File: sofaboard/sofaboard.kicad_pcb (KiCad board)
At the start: 2 copper layers, 179 parts, among them J1 USB_B_Micro, SW1 SW_Push, SW10 SW_Push, SW11 SW_Push, SW12 SW_Push, SW13 SW_Push, SW14 SW_Push, SW15 SW_Push, SW16 SW_Push, SW17 SW_Push, SW18 SW_Push, SW19 SW_Push, SW2 SW_Push, SW20 SW_Push, SW21 SW_Push, SW22 SW_Push, SW23 SW_Push, SW24 SW_Push, SW25 SW_Push, SW26 SW_Push, SW27 SW_Push, SW28 SW_Push, SW29 SW_Push, SW3 SW_Push, SW30 SW_Push, SW31 SW_Push, SW32 SW_Push, SW33 SW_Push, SW34 SW_Push, SW35 SW_Push, SW36 SW_Push, SW37 SW_Push, SW38 SW_Push, SW39 SW_Push, SW4 SW_Push, SW40 SW_Push, SW41 SW_Push, SW42 SW_Push, SW43 SW_Push, SW44 SW_Push, SW45 SW_Push, SW46 SW_Push, SW47 SW_Push, SW48 SW_Push, SW49 SW_Push, SW5 SW_Push, SW50 SW_Push, SW51 SW_Push, SW52 SW_Push, SW53 SW_Push, SW54 SW_Push, SW55 SW_Push, SW56 SW_Push, SW57 SW_Push, SW58 SW_Push, SW59 SW_Push, SW6 SW_Push, SW60 SW_Push, SW61 SW_Push, SW62 SW_Push, SW63 SW_Push, SW64 SW_Push, SW65 SW_Push, SW66 SW_Push, SW67 SW_Push, SW68 SW_Push, SW69 SW_Push, SW7 SW_Push, SW70 SW_Push, SW71 SW_Push, SW72 SW_Push, SW73 SW_Push, SW74 SW_Push, SW75 SW_Push, SW76 SW_Push, SW77 SW_Push, SW78 SW_Push, SW79 SW_Push, SW8 SW_Push, SW80 SW_Push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

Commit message: Comonent Placement
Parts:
- C1, C2, C3, C4, C5, C6, C7, C8, D1, D10, D11, D12, D13, D14, D15, D16, D17, D18, D19, D2, D20, D21, D22, D23, D24, D25, D26, D27, D28, D29, D3, D30, D31, D32, D33, D34, D35, D36, D37, D38, D39, D4, D40, D41, D42, D43, D44, D45, D46, D47, D48, D49, D5, D50, D51, D52, D53, D54, D55, D56, D57, D58, D59, D6, D60, D61, D62, D63, D64, D65, D66, D67, D68, D69, D7, D70, D71, D72, D73, D74, D75, D76, D77, D78, D79, D8, D80, D81, D82, D9, J1, R1, R2, R3, SW83, U1, Y1: moved to B.Cu
- moved R3 632.6 mm to (289.2, -111.5), turned to 90 degrees
- moved R1 619.5 mm to (285.9, -111.5), turned to 90 degrees
- moved R2 602.3 mm to (292.7, -46.0), turned to 180 degrees
- moved D14 600.2 mm to (301.4, -109.7), turned to 180 degrees
- moved C2 595.7 mm to (283.9, -68.2), turned to 270 degrees
- moved D72 588.8 mm to (282.3, -33.5), turned to 180 degrees
- moved C7 581.6 mm to (266.2, -47.3), turned to 180 degrees
- moved D43 581.5 mm to (277.3, -72.5), turned to 180 degrees
- moved D73 576.6 mm to (301.4, -33.5), turned to 180 degrees
- moved Y1 571.2 mm to (291.4, -91.9), turned to 270 degrees
- moved D13 559.1 mm to (272.7, -109.6), turned to 180 degrees
- moved D70 554.1 mm to (244.2, -33.4), turned to 180 degrees
- moved D58 553.0 mm to (301.3, -52.5), turned to 180 degrees
- moved D12 544.1 mm to (253.7, -109.7), turned to 180 degrees
- moved D44 542.6 mm to (301.3, -71.5), turned to 180 degrees
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
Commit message: Started layouting
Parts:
- moved Y1 31.9 mm to (262.7, -77.9)
- moved C7 30.7 mm to (296.9, -46.7), turned to 270 degrees
- moved R2 26.7 mm to (287.7, -72.2), turned to 90 degrees
- moved C6 24.5 mm to (294.6, -48.4)
- moved C2 22.4 mm to (267.9, -83.9), turned to 180 degrees
- moved C1 19.1 mm to (292.5, -48.4)
- moved C4 19.0 mm to (296.9, -55.4), turned to 0 degrees
- moved C5 14.7 mm to (287.1, -48.4)
- moved C3 13.6 mm to (275.2, -56.2), turned to 90 degrees
- moved C8 13.5 mm to (290.3, -48.4)
- moved SW83 11.8 mm to (291.0, -81.9)
- moved U1 2.45 mm to (285.9, -59.6), turned to 90 degrees
- moved R3 1.15 mm to (288.1, -111.5)
- moved R1 0.20 mm to (286.1, -111.5)
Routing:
- net row1: track 0.00 -> 553.8 mm, vias 0 -> 2
- net row3: track 0.00 -> 468.8 mm, vias 0 -> 2
- net row5: track 0.00 -> 453.1 mm, vias 0 -> 2
- net row0: track 0.00 -> 411.5 mm, vias 0 -> 2
- net row2: track 0.00 -> 399.2 mm, vias 0 -> 2
- net col0: track 0.00 -> 368.0 mm, vias 0 -> 2
- net col1: track 0.00 -> 353.9 mm, vias 0 -> 5
- net row4: track 0.00 -> 342.1 mm
- net col2: track 0.00 -> 337.2 mm, vias 0 -> 3
- net col6: track 0.00 -> 319.7 mm, vias 0 -> 4
- net col5: track 0.00 -> 303.6 mm, vias 0 -> 3
- net col3: track 0.00 -> 301.8 mm, vias 0 -> 5
- net col4: track 0.00 -> 268.4 mm, vias 0 -> 1
- net col7: track 0.00 -> 256.2 mm, vias 0 -> 4
- net col10: track 0.00 -> 236.4 mm, vias 0 -> 1
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
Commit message: Optimised routing
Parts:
- moved SW83 174.2 mm to (129.4, -16.8)
- moved C4 137.0 mm to (165.9, -15.2), turned to 180 degrees
- moved C2 127.6 mm to (152.5, -29.6), turned to 270 degrees
- moved C5 124.0 mm to (166.0, -21.8), turned to 180 degrees
- moved C3 119.9 mm to (161.3, -18.6), turned to 270 degrees
- moved Y1 119.6 mm to (156.7, -22.7)
- moved U1 113.3 mm to (178.6, -23.0), turned to 0 degrees
- moved R2 110.2 mm to (190.2, -21.1), turned to 0 degrees
- moved C7 105.7 mm to (194.4, -21.1), turned to 0 degrees
- moved C6 104.5 mm to (194.4, -18.9), turned to 0 degrees
- moved C1 103.1 mm to (194.4, -16.8), turned to 0 degrees
- moved C8 101.7 mm to (194.4, -14.6), turned to 0 degrees
- moved J1 86.1 mm to (201.0, -118.4)
- moved R1 86.1 mm to (200.0, -110.7)
- moved R3 86.1 mm to (202.0, -110.7)
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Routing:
- net col5: track 303.6 -> 139.8 mm, vias 3 -> 1
- net col6: track 319.7 -> 163.6 mm, vias 4 -> 1
- net col7: track 256.2 -> 114.6 mm, vias 4 -> 1
- net col8: track 204.5 -> 95.2 mm, vias 4 -> 0
- net col3: track 301.8 -> 196.9 mm, vias 5 -> 1
- net col14: track 122.3 -> 225.4 mm, vias 2 -> 0
- net col2: track 337.2 -> 235.0 mm, vias 3 -> 1
- net col1: track 353.9 -> 252.8 mm, vias 5 -> 0
- net col10: track 236.4 -> 138.9 mm
- net col0: track 368.0 -> 272.8 mm, vias 2 -> 1
- net col4: track 268.4 -> 179.7 mm
- net col9: track 206.8 -> 119.4 mm, vias 3 -> 1
- net Net-(R3-Pad1): track 65.1 -> 150.5 mm
- net Net-(R1-Pad1): track 63.4 -> 146.6 mm
- net col13: track 122.3 -> 204.1 mm, vias 0 -> 1
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
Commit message: Added GND planes
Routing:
- net +5V: track 53.2 -> 152.8 mm, vias 0 -> 4
- net GND: track 0.00 -> 13.0 mm, vias 0 -> 25
- net (no net): vias 0 -> 1
- added copper zone on B.Cu, net GND
- added copper zone on F.Cu, net GND
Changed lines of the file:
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@@
     (thickness 1.6)
     (drawings 364)
-    (tracks 957)
+    (tracks 1014)
     (zones 0)
     (modules 179)
@@
     (0 F.Cu signal)
     (31 B.Cu signal)
-    (32 B.Adhes user hide)
-    (33 F.Adhes user hide)
-    (34 B.Paste user hide)
-    (35 F.Paste user hide)
-    (36 B.SilkS user hide)
-    (37 F.SilkS user hide)
-    (38 B.Mask user hide)
-    (39 F.Mask user hide)
-    (40 Dwgs.User user hide)
-    (41 Cmts.User user hide)
-    (42 Eco1.User user hide)
-    (43 Eco2.User user hide)
-    (44 Edge.Cuts user hide)
-    (45 Margin user hide)
-    (46 B.CrtYd user hide)
-    (47 F.CrtYd user hide)
-    (48 B.Fab user hide)
-    (49 F.Fab user hide)
+    (32 B.Adhes user)
+    (33 F.Adhes user)
+    (34 B.Paste user)
+    (35 F.Paste user)
+    (36 B.SilkS user)
+    (37 F.SilkS user)
+    (38 B.Mask user)
+    (39 F.Mask user)
+    (40 Dwgs.User user)
+    (41 Cmts.User user)
+    (42 Eco1.User user)
+    (43 Eco2.User user)
+    (44 Edge.Cuts user)
+    (45 Margin user)
+    (46 B.CrtYd user)
+    (47 F.CrtYd user)
+    (48 B.Fab user)
+    (49 F.Fab user)
   )
   (setup
@@
   (gr_line (start 122.841 -121.9501) (end 136.842 -121.9501) (layer Dwgs.User) (width 0.2))
   (gr_line (start 227.33 -50.8) (end 213.33 -50.8) (layer Dwgs.User) (width 0.2))
+  (via (at 179.29 -22.57) (size 0.8) (drill 0.4) (layers F.Cu B.Cu) (net 0))
   (segment (start 193.36 -18.945) (end 193.335 -18.92) (width 0.25) (layer B.Cu) (net 1))
   (segment (start 193.36 -21.05) (end 193.36 -18.945) (width 0.25) (layer B.Cu) (net 1))
@@
   (segment (start 193.34 -16.765) (end 193.355 -16.78) (width 0.25) (layer B.Cu) (net 1))
   (segment (start 193.34 -14.59) (end 193.34 -16.765) (width 0.25) (layer B.Cu) (net 1))
+  (via (at 176.69 -37.5) (size 0.8) (drill 0.4) (layers F.Cu B.Cu) (net 1))
+  (segment (start 175.83 -30.73) (end 175.83 -36.64) (width 0.25) (layer B.Cu) (net 1))
+  (segment (start 175.83 -36.64) (end 176.69 -37.5) (width 0.25) (layer B.Cu) (net 1))
+  (via (at 187.52 -81.27) (size 0.8) (drill 0.4) (layers F.Cu B.Cu) (net 1))
+  (segment (start 187.52 -43.510998) (end 187.52 -81.27) (width 0.25) (layer F.Cu) (net 1))
+  (segment (start 176.69 -37.5) (end 181.509002 -37.5) (width 0.25) (layer F.Cu) (net 1))
+  (segment (start 181.509002 -37.5) (end 187.52 -43.510998) (width 0.25) (layer F.Cu) (net 1))
+  (segment (start 187.52 -81.27) (end 193.89 -87.64) (width 0.25) (layer B.Cu) (net 1))
+  (via (at 192.69 -102.84) (size 0.8) (drill 0.4) (layers F.Cu B.Cu) (net 1))
+  (segment (start 193.89 -87.64) (end 193.89 -101.64) (width 0.25) (layer B.Cu) (net 1))
+  (segment (start 193.89 -101.64) (end 192.69 -102.84) (width 0.25) (layer B.Cu) (net 1))
+  (via (at 198.23 -113.23) (size 0.8) (drill 0.4) (layers F.Cu B.Cu) (net 1))
+  (segment (start 192.69 -102.84) (end 198.23 -108.38) (width 0.25) (layer F.Cu) (net 1))
+  (segment (start 198.23 -108.38) (end 198.23 -113.23) (width 0.25) (layer F.Cu) (net 1))
+  (segment (start 199.67 -114.67) (end 199.67 -116.64) (width 0.25) (layer B.Cu) (net 1))
+  (segment (start 198.23 -113.23) (end 199.67 -114.67) (width 0.25) (layer B.Cu) (net 1))
+  (via (at 150.14 -20.2) (size 0.8) (drill 0.4) (layers F.Cu B.Cu) (net 2))
+  (via (at 160.47 -21.73) (size 0.8) (drill 0.4) (layers F.Cu B.Cu) (net 2))
+  (via (at 172.8 -37.19) (size 0.8) (drill 0.4) (layers F.Cu B.Cu) (net 2))
+  (segment (start 176.63 -31.73) (end 176.6 -31.76) (width 0.25) (layer B.Cu) (net 2))
+  (segment (start 176.63 -30.73) (end 176.63 -31.73) (width 0.25) (layer B.Cu) (net 2))
+  (via (at 179.54 -18.15) (size 0.8) (drill 0.4) (layers F.Cu B.Cu) (net 2))
+  (segment (start 181.43 -15.33) (end 181.43 -16.91) (width 0.25) (layer B.Cu) (net 2))
+  (via (at 180.02 -26.42) (size 0.8) (drill 0.4) (layers F.Cu B.Cu) (net 2))
+  (via (at 174.04 -26.26) (size 0.8) (drill 0.4) (layers F.Cu B.Cu) (net 2))
+  (segment (start 173.43 -16.33) (end 173.42 -16.34) (width 0.25) (layer B.Cu) (net 2))
+  (segment (start 173.43 -15.33) (end 173.43 -16.33) (width 0.25) (layer B.Cu) (net 2))
+  (segment (start 173.43 -16.33) (end 173.43 -16.79) (width 0.25) (layer B.Cu) (net 2))
+  (segment (start 169.93 -21.03) (end 169.68 -20.78) (width 0.25) (layer B.Cu) (net 2))
+  (segment (start 170.93 -21.03) (end 169.93 -21.03) (width 0.25) (layer B.Cu) (net 2))
+  (segment (start 169.68 -20.78) (end 165.02 -20.78) (width 0.25) (layer B.Cu) (net 2))
+  (segment (start 164.965 -20.835) (end 164.965 -21.83) (width 0.25) (layer B.Cu) (net 2))
+  (segment (start 165.02 -20.78) (end 164.965 -20.835) (width 0.25) (layer B.Cu) (net 2))
+  (segment (start 165.02 -20.78) (end 164.94 -20.78) (width 0.25) (layer B.Cu) (net 2))
+  (segment (start 176.63 -29.73) (end 176.64 -29.72) (width 0.25) (layer B.Cu) (net 2))
+  (segment (start 176.63 -30.73) (end 176.63 -29.73) (width 0.25) (layer B.Cu) (net 2))
+  (segment (start 176.64 -29.72) (end 176.64 -28.98) (width 0.25) (layer B.Cu) (net 2))
+  (via (at 188.87 -15.25) (size 0.8) (drill 0.4) (layers F.Cu B.Cu) (net 2))
+  (via (at 190.92 -17.76) (size 0.8) (drill 0.4) (layers F.Cu B.Cu) (net 2))
+  (via (at 158.98 -15.54) (size 0.8) (drill 0.4) (layers F.Cu B.Cu) (net 2))
+  (via (at 158.9 -18.06) (size 0.8) (drill 0.4) (layers F.Cu B.Cu) (net 2))
+  (via (at 190.79 -32.93) (size 0.8) (drill 0.4) (layers F.Cu B.Cu) (net 2))
+  (via (at 228.92 -22.65) (size 0.8) (drill 0.4) (layers F.Cu B.Cu) (net 2))
+  (via (at 251.56 -22.73) (size 0.8) (drill 0.4) (layers F.Cu B.Cu) (net 2))
+  (via (at 272.28 -23.4) (size 0.8) (drill 0.4) (layers F.Cu B.Cu) (net 2))
+  (via (at 290.75 -22.49) (size 0.8) (drill 0.4) (layers F.Cu B.Cu) (net 2))
+  (via (at 32.07 -23.6) (size 0.8) (drill 0.4) (layers F.Cu B.Cu) (net 2))
+  (via (at 51.96 -23.16) (size 0.8) (drill 0.4) (layers F.Cu B.Cu) (net 2))
+  (via (at 151.69 -14.03) (size 0.8) (drill 0.4) (layers F.Cu B.Cu) (net 2))
+  (via (at 197.28 -68.53) (size 0.8) (drill 0.4) (layers F.Cu B.Cu) (net 2))
+  (via (at 195.27 -86.68) (size 0.8) (drill 0.4) (layers F.Cu B.Cu) (net 2))
+  (via (at 201.69 -47.93) (size 0.8) (drill 0.4) (layers F.Cu B.Cu) (net 2))
+  (via (at 206.06 -34.07) (size 0.8) (drill 0.4) (layers F.Cu B.Cu) (net 2))
+  (via (at 176.2 -22.38) (size 0.8) (drill 0.4) (layers F.Cu B.Cu) (net 2))
+  (via (at 182.3 -27.29) (size 0.8) (drill 0.4) (layers F.Cu B.Cu) (net 2))
+  (via (at 181.23 -23.03) (size 0.8) (drill 0.4) (layers F.Cu B.Cu) (net 2))
   (via (at 159.75 -27.48) (size 0.8) (drill 0.4) (layers F.Cu B.Cu) (net 3))
   (segment (start 175.71 -25.08) (end 178.23 -27.6) (width 0.25) (layer B.Cu) (net 3))
@@
   (segment (start 174.37 -32.924315) (end 175.03 -32.264315) (width 0.25) (layer B.Cu) (net 116))
   (segment (start 174.37 -33.49) (end 174.37 -32.924315) (width 0.25) (layer B.Cu) (net 116))
+  (zone (net 2) (net_name GND) (layer F.Cu) (hatch edge 0.508)
+    (connect_pads (clearance 0.508))
+    (min_thickness 0.254)
+    (fill yes (arc_segments 16) (thermal_gap 0.508) (thermal_bridge_width 0.508))
+    (polygon
+      (pts
+        (xy 8.522552 -121.92136) (xy 308.29 -121.97) (xy 308.29 -12.67) (xy 8.48 -12.7)
+      )
+    )
+  )
+  (zone (net 2) (net_name GND) (layer B.Cu) (hatch edge 0.508)
+    (connect_pads (clearance 0.508))
+    (min_thickness 0.254)
+    (fill yes (arc_segments 16) (thermal_gap 0.508) (thermal_bridge_width 0.508))
+    (polygon
+      (pts
+        (xy 8.55 -121.92) (xy 308.28 -121.93) (xy 308.27 -12.71) (xy 8.44 -12.62)
+      )
+    )
+  )
 )

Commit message: Progress
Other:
- board outline added: 300 x 109.6 mm

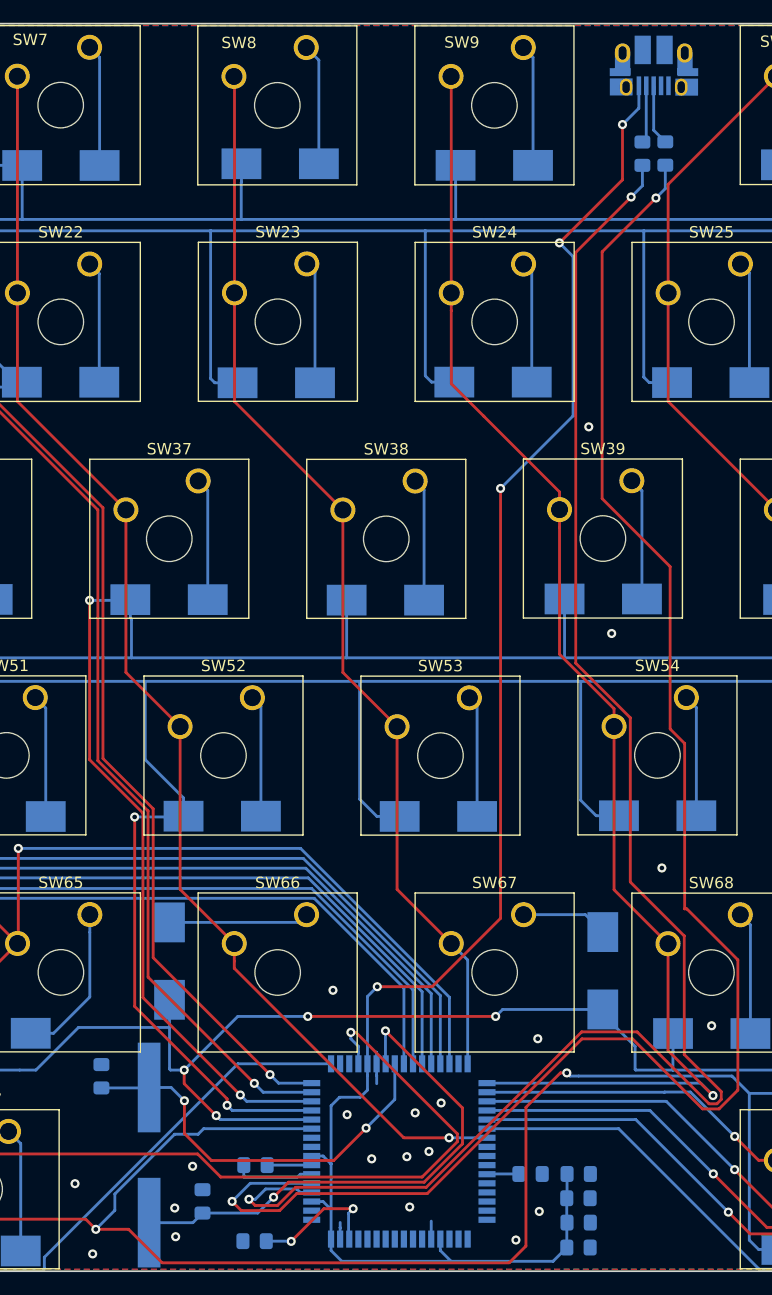
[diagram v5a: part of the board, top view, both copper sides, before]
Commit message: Change crystal footprint
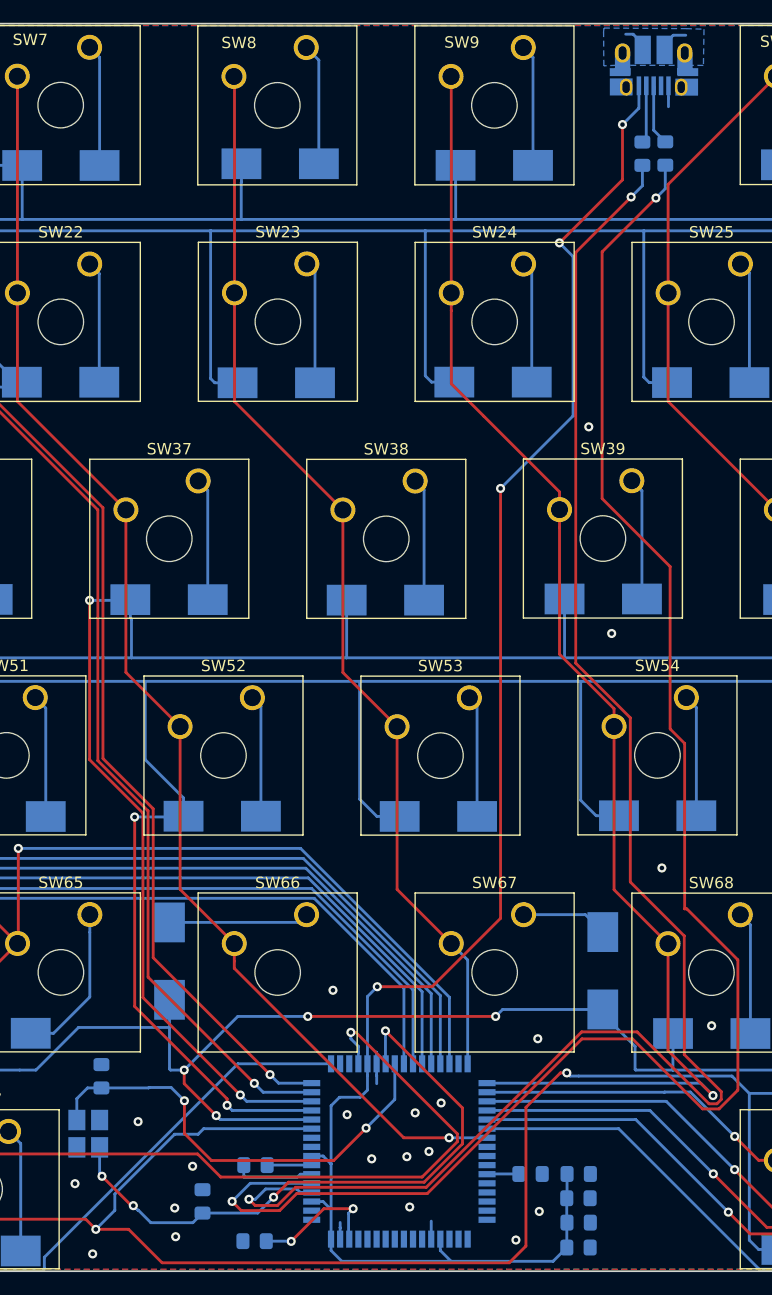
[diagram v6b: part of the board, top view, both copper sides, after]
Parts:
- Y1: footprint Crystal:Crystal_SMD_HC49-SD_HandSoldering -> Cherry:Crytal16
- moved Y1 4.40 mm to (152.3, -23.4), turned to 90 degrees
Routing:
- net Net-(C3-Pad2): track 46.0 -> 54.5 mm, vias 2 -> 4
- net GND: track 13.0 -> 19.9 mm, vias 25 -> 26
- net Net-(C2-Pad2): track 35.5 -> 39.9 mm

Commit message: Changed crytal fp and added vias
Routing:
- net GND: vias 26 -> 207

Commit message: Made ready for ordering
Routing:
- net GND: vias 207 -> 209
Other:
- board size 300 x 109.6 mm -> 301 x 111.8 mm
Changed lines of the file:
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@@
     (thickness 1.6)
     (drawings 360)
-    (tracks 1216)
+    (tracks 1218)
     (zones 0)
     (modules 179)
@@
     (0 F.Cu signal)
     (31 B.Cu signal)
-    (32 B.Adhes user hide)
-    (33 F.Adhes user hide)
-    (34 B.Paste user hide)
-    (35 F.Paste user hide)
+    (32 B.Adhes user)
+    (33 F.Adhes user)
+    (34 B.Paste user)
+    (35 F.Paste user)
     (36 B.SilkS user)
-    (37 F.SilkS user hide)
-    (38 B.Mask user hide)
-    (39 F.Mask user hide)
-    (40 Dwgs.User user hide)
-    (41 Cmts.User user hide)
-    (42 Eco1.User user hide)
-    (43 Eco2.User user hide)
-    (44 Edge.Cuts user hide)
-    (45 Margin user hide)
-    (46 B.CrtYd user hide)
-    (47 F.CrtYd user hide)
-    (48 B.Fab user hide)
-    (49 F.Fab user hide)
+    (37 F.SilkS user)
+    (38 B.Mask user)
+    (39 F.Mask user)
+    (40 Dwgs.User user)
+    (41 Cmts.User user)
+    (42 Eco1.User user)
+    (43 Eco2.User user)
+    (44 Edge.Cuts user)
+    (45 Margin user)
+    (46 B.CrtYd user)
+    (47 F.CrtYd user)
+    (48 B.Fab user)
+    (49 F.Fab user)
   )
   (setup
@@
     (visible_elements FFFFFF7F)
     (pcbplotparams
-      (layerselection 0x010f0_ffffffff)
+      (layerselection 0x030fc_ffffffff)
       (usegerberextensions true)
       (usegerberattributes false)
@@
     )
   )
-  (gr_line (start 8.39 -12.51) (end 8.39 -122.09) (layer Edge.Cuts) (width 0.15))
-  (gr_line (start 308.37 -12.51) (end 8.39 -12.51) (layer Edge.Cuts) (width 0.15))
-  (gr_line (start 308.37 -122.1) (end 308.37 -12.51) (layer Edge.Cuts) (width 0.15))
-  (gr_line (start 8.4 -122.1) (end 308.37 -122.1) (layer Edge.Cuts) (width 0.15))
+  (gr_line (start 7.62 -11.43) (end 7.62 -123.19) (layer Edge.Cuts) (width 0.15))
+  (gr_line (start 308.61 -11.43) (end 7.62 -11.43) (layer Edge.Cuts) (width 0.15))
+  (gr_line (start 308.61 -123.19) (end 308.61 -11.43) (layer Edge.Cuts) (width 0.15))
+  (gr_line (start 7.62 -123.19) (end 308.61 -123.19) (layer Edge.Cuts) (width 0.15))
   (gr_line (start 227.33 -50.8) (end 213.33 -50.8) (layer Dwgs.User) (width 0.2))
   (gr_line (start 122.841 -121.9501) (end 136.842 -121.9501) (layer Dwgs.User) (width 0.2))
@@
   (via (at 295 -39) (size 0.8) (drill 0.4) (layers F.Cu B.Cu) (net 2))
   (via (at 78 -20) (size 0.8) (drill 0.4) (layers F.Cu B.Cu) (net 2))
-  (via (at 88 -20) (size 0.8) (drill 0.4) (layers F.Cu B.Cu) (net 2))
-  (via (at 97 -20) (size 0.8) (drill 0.4) (layers F.Cu B.Cu) (net 2))
-  (via (at 107 -20) (size 0.8) (drill 0.4) (layers F.Cu B.Cu) (net 2))
   (via (at 118 -20) (size 0.8) (drill 0.4) (layers F.Cu B.Cu) (net 2))
   (via (at 201 -17) (size 0.8) (drill 0.4) (layers F.Cu B.Cu) (net 2))
+  (via (at 85.09 -19.05) (size 0.8) (drill 0.4) (layers F.Cu B.Cu) (net 2))
+  (via (at 111.76 -19.05) (size 0.8) (drill 0.4) (layers F.Cu B.Cu) (net 2))
+  (via (at 105.41 -21.59) (size 0.8) (drill 0.4) (layers F.Cu B.Cu) (net 2))
+  (via (at 91.44 -21.59) (size 0.8) (drill 0.4) (layers F.Cu B.Cu) (net 2))
+  (via (at 99.06 -20.32) (size 0.8) (drill 0.4) (layers F.Cu B.Cu) (net 2))
   (via (at 159.75 -27.48) (size 0.8) (drill 0.4) (layers F.Cu B.Cu) (net 3))
   (segment (start 152.46 -28.61) (end 156.6125 -28.61) (width 0.25) (layer B.Cu) (net 3))
@@
     (polygon
       (pts
-        (xy 8.522552 -121.92136) (xy 308.29 -121.97) (xy 308.29 -12.67) (xy 8.48 -12.7)
+        (xy 7.62 -123.19) (xy 308.61 -123.19) (xy 308.61 -11.43) (xy 7.62 -11.43)
       )
     )
@@
     (polygon
       (pts
-        (xy 8.55 -121.92) (xy 308.28 -121.93) (xy 308.27 -12.71) (xy 8.44 -12.62)
+        (xy 7.62 -123.19) (xy 308.61 -123.19) (xy 308.61 -11.43) (xy 7.62 -11.43)
       )
     )
